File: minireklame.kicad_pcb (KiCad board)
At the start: 2 copper layers, 100 x 50 mm, 62 parts, among them IC1 ATXMEGA64A4U-A, P1 CONN_01X04, P10 CONN_01X04, P11 CONN_01X04, P12 CONN_01X04, P13 CONN_01X04, P14 CONN_01X04, P15 CONN_01X04, P16 CONN_01X04, P17 Screw_Terminal_1x02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

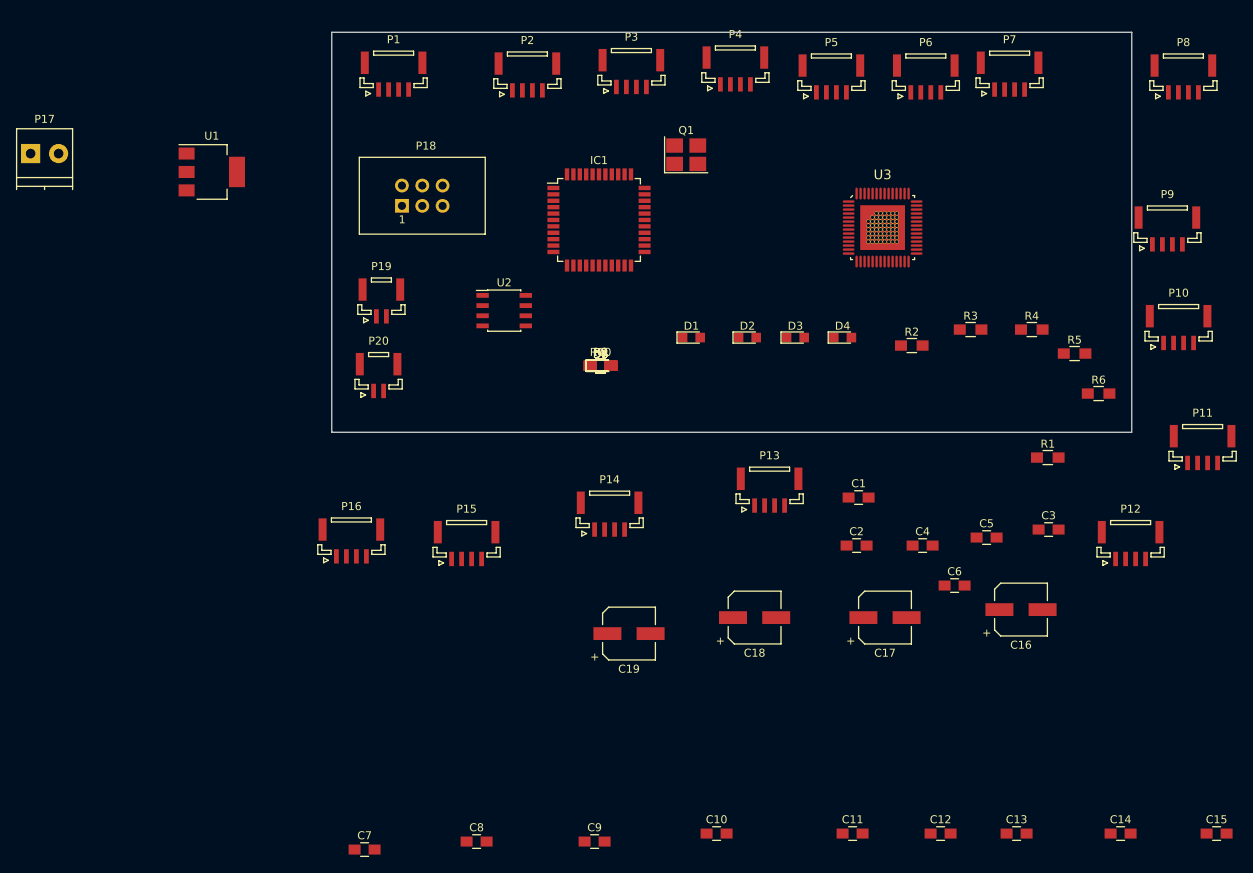
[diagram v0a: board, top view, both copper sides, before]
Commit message: arranging parts roughly in board outline
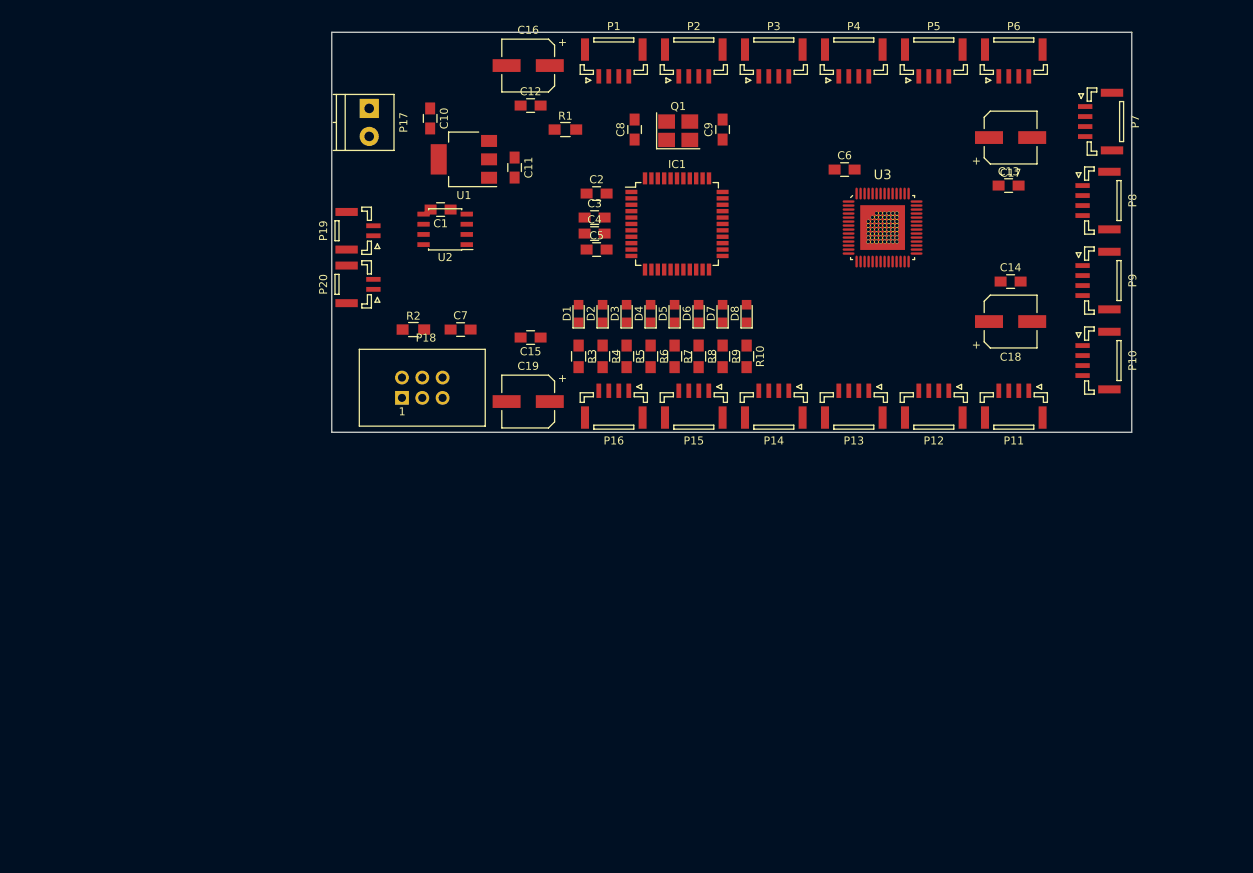
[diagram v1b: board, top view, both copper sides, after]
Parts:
- moved C15 105.8 mm to (94.9, 88.2), turned to 180 degrees
- moved C12 104.4 mm to (94.9, 59.2)
- moved C10 96.3 mm to (82.3, 60.8), turned to 270 degrees
- moved C11 93.4 mm to (92.9, 66.9), turned to 270 degrees
- moved C16 91.8 mm to (94.6, 54.2), turned to 180 degrees
- moved C8 91.2 mm to (107.9, 62.2), turned to 90 degrees
- moved C9 90.4 mm to (118.9, 62.2), turned to 90 degrees
- moved C13 81.0 mm to (154.6, 69.2)
- moved R1 72.9 mm to (99.2, 62.2)
- moved C14 70.4 mm to (154.9, 81.2)
- moved C3 68.9 mm to (102.9, 73.2)
- moved C7 66.1 mm to (86.1, 87.2)
- moved C1 63.5 mm to (83.6, 72.2), turned to 180 degrees
- moved R2 62.3 mm to (80.2, 87.2)
- moved C17 62.0 mm to (154.9, 63.2)
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
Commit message: merging VDD and +5V net
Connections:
- C10 pad 1: VDD -> +5V
- P17 pad 1: VDD -> +5V
- U1 pad 3: VDD -> +5V

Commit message: starting to route stuff...
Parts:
- Q1: value Crystal -> Crystal_GND24
- moved P16 66.5 mm to (156.0, 53.6), turned to 0 degrees
- moved P9 59.2 mm to (108.4, 96.4), turned to 180 degrees
- moved P2 53.2 mm to (166.4, 68.4), turned to 270 degrees
- moved P14 47.4 mm to (105.2, 53.6), turned to 0 degrees
- moved P3 44.9 mm to (138.9, 96.6), turned to 180 degrees
- moved P1 44.8 mm to (118.6, 96.6), turned to 180 degrees
- moved P15 44.1 mm to (125.5, 53.6), turned to 0 degrees
- moved P5 42.9 mm to (149.0, 96.6), turned to 180 degrees
- moved P13 35.8 mm to (166.3, 78.6), turned to 270 degrees
- moved P10 32.8 mm to (166.4, 58.2)
- moved R10 32.5 mm to (98.5, 67.9)
- moved D8 32.2 mm to (98.5, 63.1)
- moved C8 28.9 mm to (125.2, 85.2)
- moved R9 28.8 mm to (101.1, 67.9)
- moved D7 28.4 mm to (101.1, 63.1)
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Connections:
- Q1 pad 2: Net-(C9-Pad1) -> GND
- Q1 pad 3: (no net) -> Net-(C9-Pad1)
- Q1 pad 4: (no net) -> GND
- U3 pad 24: Net-(P15-Pad3) -> Net-(P15-Pad2)
- U3 pad 25: Net-(P15-Pad2) -> Net-(P15-Pad3)
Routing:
- net +3V3: track 0.00 -> 106.7 mm
- net Net-(C7-Pad1): track 0.00 -> 47.4 mm
- net Net-(P9-Pad3): track 0.00 -> 47.1 mm
- net Net-(P9-Pad2): track 0.00 -> 43.7 mm
- net Net-(P14-Pad3): track 0.00 -> 42.9 mm
- net Net-(P9-Pad1): track 0.00 -> 42.2 mm
- net +5V: track 0.00 -> 41.3 mm
- net Net-(P14-Pad1): track 0.00 -> 39.3 mm
- net Net-(P14-Pad2): track 0.00 -> 38.2 mm
- net Net-(IC1-Pad34): track 0.00 -> 36.1 mm
- net Net-(P12-Pad3): track 0.00 -> 34.2 mm
- net Net-(P10-Pad3): track 0.00 -> 34.1 mm
- net Net-(P1-Pad3): track 0.00 -> 33.5 mm
- net Net-(P4-Pad3): track 0.00 -> 32.9 mm
- net Net-(P12-Pad2): track 0.00 -> 31.7 mm
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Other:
- net class pwr: trace_width 0.5 -> 0.25
- net class small added: clearance 0.1524, trace_width 0.1524, via_dia 0.6, via_drill 0.4
- rule trace_min: 0.2 -> 0.1524

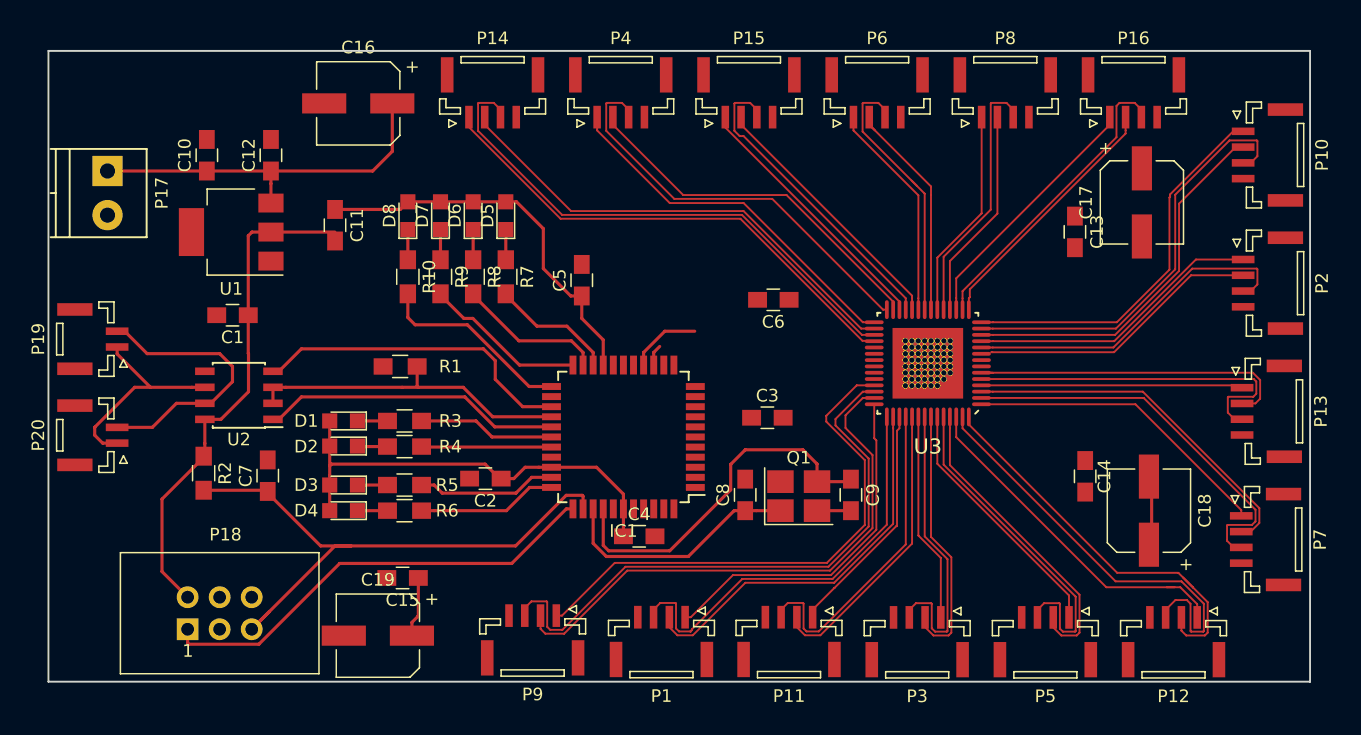
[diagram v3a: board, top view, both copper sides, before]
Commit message: routing top layer finished, ground conn missing
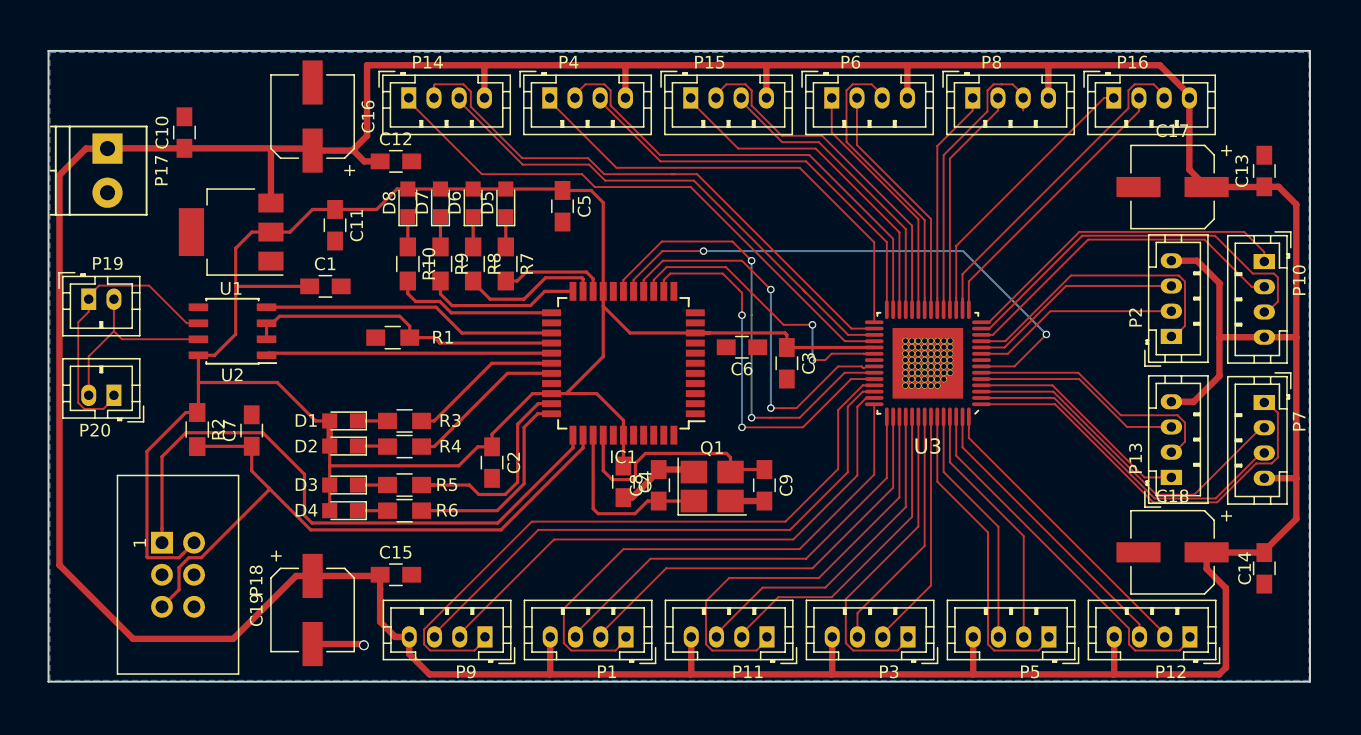
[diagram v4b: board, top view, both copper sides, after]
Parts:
- P1, P10, P11, P12, P13, P14, P15, P16, P2, P3, P4, P5, P6, P7, P8, P9: footprint Connectors_JST:JST_GH_BM04B-GHS-TBT_04x1.25mm_Straight -> Connectors_JST:JST_PH_B4B-PH-K_04x2.00mm_Straight
- P19, P20: footprint Connectors_JST:JST_GH_BM02B-GHS-TBT_02x1.25mm_Straight -> Connectors_JST:JST_PH_B2B-PH-K_02x2.00mm_Straight
- moved C14 16.0 mm to (166.4, 91.0), turned to 270 degrees
- moved C13 15.8 mm to (166.4, 59.5), turned to 90 degrees
- moved P7 10.9 mm to (166.4, 77.9)
- moved C12 9.92 mm to (97.5, 58.8), turned to 0 degrees
- moved P13 8.97 mm to (159.0, 83.8), turned to 90 degrees
- moved P2 8.49 mm to (159.0, 72.6), turned to 90 degrees
- moved P10 8.45 mm to (166.4, 66.7)
- moved C1 7.71 mm to (92.0, 68.7), turned to 0 degrees
- moved P18 7.15 mm to (79.0, 89.0), turned to 270 degrees
- moved C8 6.90 mm to (118.4, 84.4)
- moved C9 6.90 mm to (126.8, 84.4)
- moved Q1 6.90 mm to (122.6, 84.5)
- moved P14 6.65 mm to (98.6, 53.7)
- moved C5 6.06 mm to (110.7, 62.3), turned to 270 degrees
- moved IC1 5.84 mm to (115.6, 74.8)
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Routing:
- net +5V: track 41.3 -> 350.7 mm
- net +3V3: track 106.7 -> 162.1 mm
- net Net-(IC1-Pad16): track 0.00 -> 43.5 mm, vias 0 -> 2
- net Net-(IC1-Pad17): track 0.00 -> 36.6 mm, vias 0 -> 2
- net Net-(IC1-Pad13): track 0.00 -> 30.7 mm, vias 0 -> 2
- net Net-(IC1-Pad15): track 5.75 -> 30.8 mm, vias 0 -> 2
- net Net-(IC1-Pad14): track 1.67 -> 23.7 mm, vias 0 -> 2
- net Net-(P11-Pad1): track 18.8 -> 34.2 mm
- net Net-(P1-Pad1): track 28.0 -> 43.1 mm
- net Net-(IC1-Pad34): track 36.1 -> 49.1 mm
- net Net-(P13-Pad3): track 27.8 -> 16.6 mm
- net Net-(P9-Pad1): track 42.2 -> 53.2 mm
- net Net-(P12-Pad3): track 34.2 -> 23.3 mm
- net GND: track 2.97 -> 13.5 mm, vias 0 -> 1
- net Net-(C9-Pad1): track 29.2 -> 18.8 mm
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- added copper zone on B.Cu, net GND
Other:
- net class Default: trace_width 0.25 -> 0.254
- net class pwr: clearance 0.4 -> 0.2; trace_width 0.25 -> 0.508; via_dia 0.6 -> 0.8; via_drill 0.4 -> 0.6

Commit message: finalising review version of pcb layout
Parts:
- moved P17 0.56 mm to (74.7, 58.3)
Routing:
- net GND: track 13.5 -> 125.6 mm, vias 1 -> 21
- net Net-(IC1-Pad16): track 43.5 -> 48.6 mm
- net +3V3: track 162.1 -> 164.4 mm
- net +5V: track 350.7 -> 349.7 mm
- net Net-(IC1-Pad15): track 30.8 -> 31.6 mm
- net Net-(IC1-Pad14): track 23.7 -> 23.0 mm
- added copper zone on F.Cu, net GND

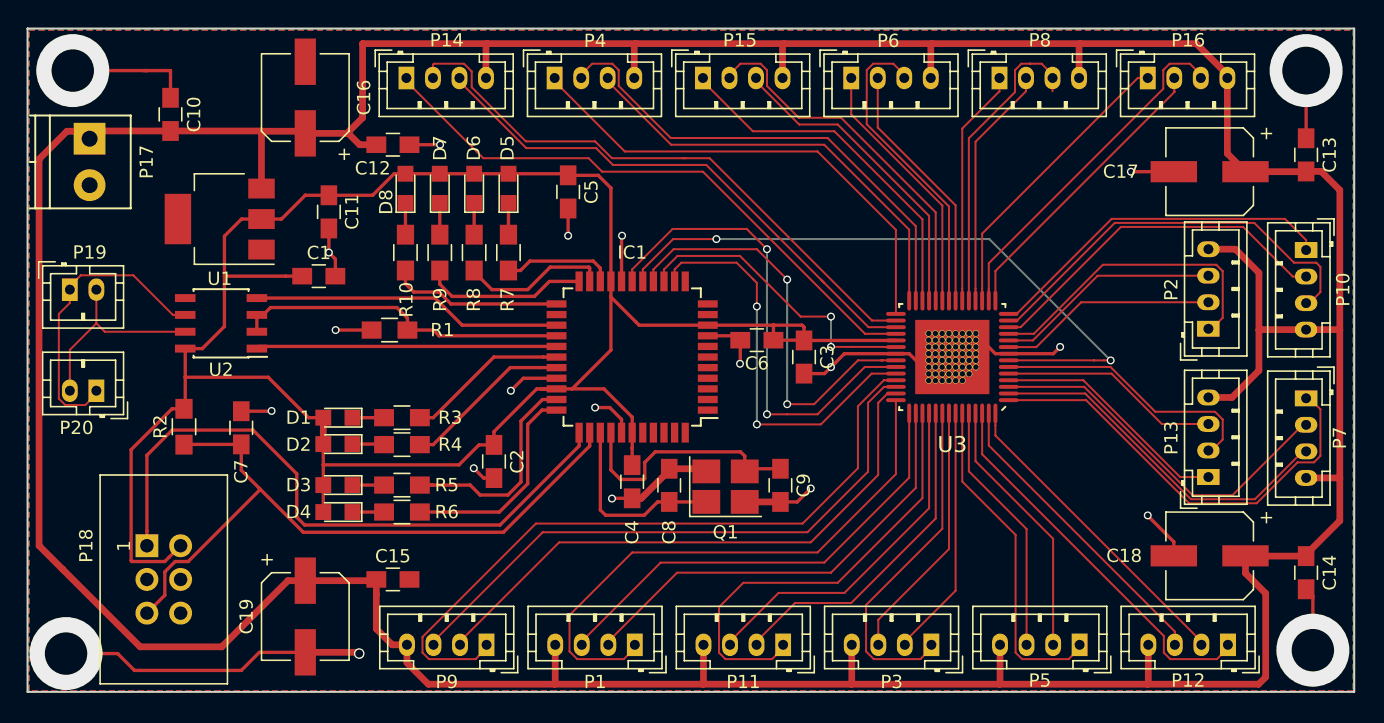
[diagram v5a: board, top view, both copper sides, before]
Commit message: chainging track width out of TCL5955 and distributing traces better
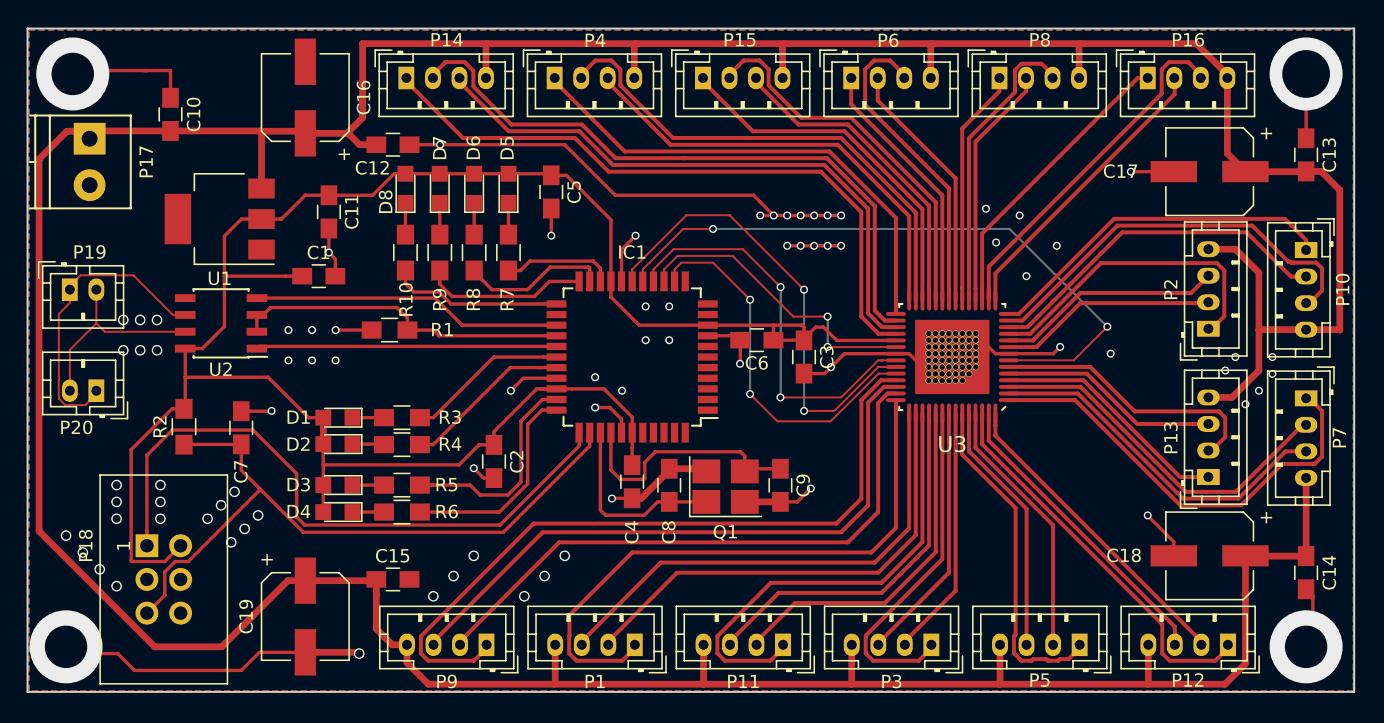
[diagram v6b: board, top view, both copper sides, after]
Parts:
- moved C5 1.27 mm to (109.5, 62.3)
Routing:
- net GND: track 125.6 -> 163.5 mm, vias 21 -> 84
- net +5V: track 349.7 -> 331.5 mm
- net +3V3: track 164.4 -> 155.7 mm
- net Net-(P14-Pad1): track 45.0 -> 49.6 mm
- net Net-(P14-Pad3): track 41.2 -> 45.5 mm
- net Net-(P14-Pad2): track 44.9 -> 49.2 mm
- net Net-(P1-Pad1): track 43.1 -> 45.7 mm
- net Net-(IC1-Pad13): track 30.7 -> 28.4 mm
- net Net-(P1-Pad3): track 34.9 -> 37.1 mm
- net Net-(P1-Pad2): track 33.8 -> 35.9 mm
- net Net-(P9-Pad1): track 53.2 -> 55.3 mm
- net Net-(P11-Pad3): track 26.6 -> 28.2 mm
- net Net-(P9-Pad2): track 44.0 -> 45.7 mm
- net Net-(P11-Pad2): track 25.5 -> 27.0 mm
- net Net-(P9-Pad3): track 46.1 -> 47.6 mm
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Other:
- net class led added: clearance 0.2, trace_width 0.3, via_dia 0.6, via_drill 0.4
